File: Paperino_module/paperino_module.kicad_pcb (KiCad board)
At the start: 2 copper layers, 25.4 x 22 mm, 21 parts, among them P1 CONN_01X06, P2 CONN_01X06, P3 CONN_01X06, P4 CONN_01X06, Q1 PMOS, Q2 NMOS, U1 BMA250E, X1 XF2M-2615-1A, X2 XF2B-4545-1A

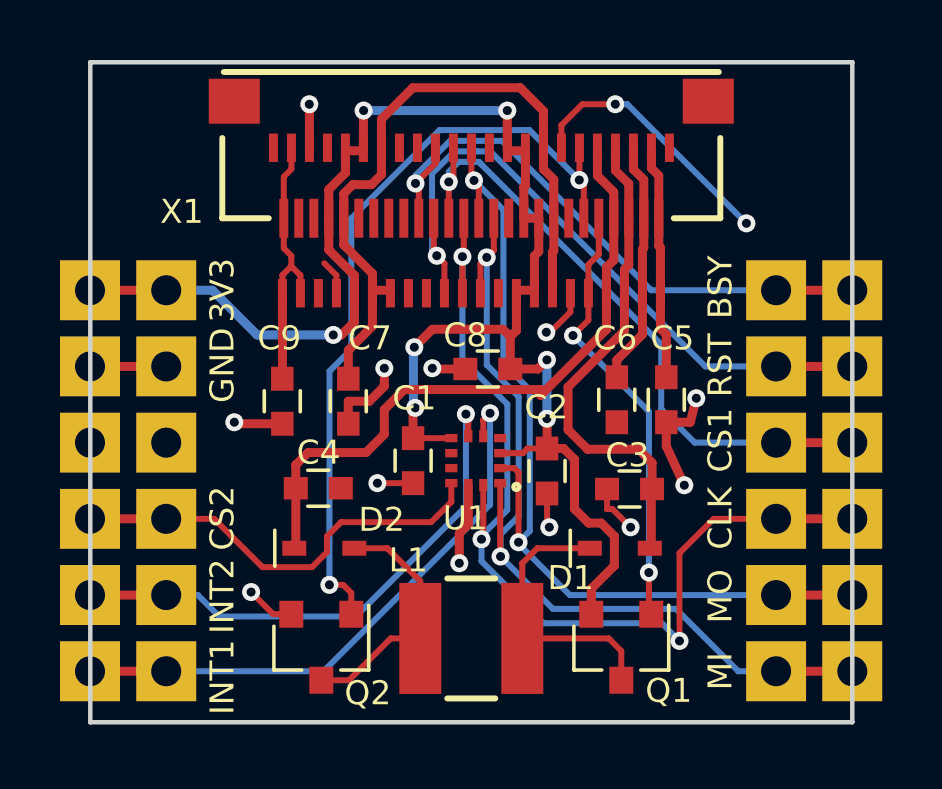
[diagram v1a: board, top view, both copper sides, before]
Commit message: more robust design for castellation
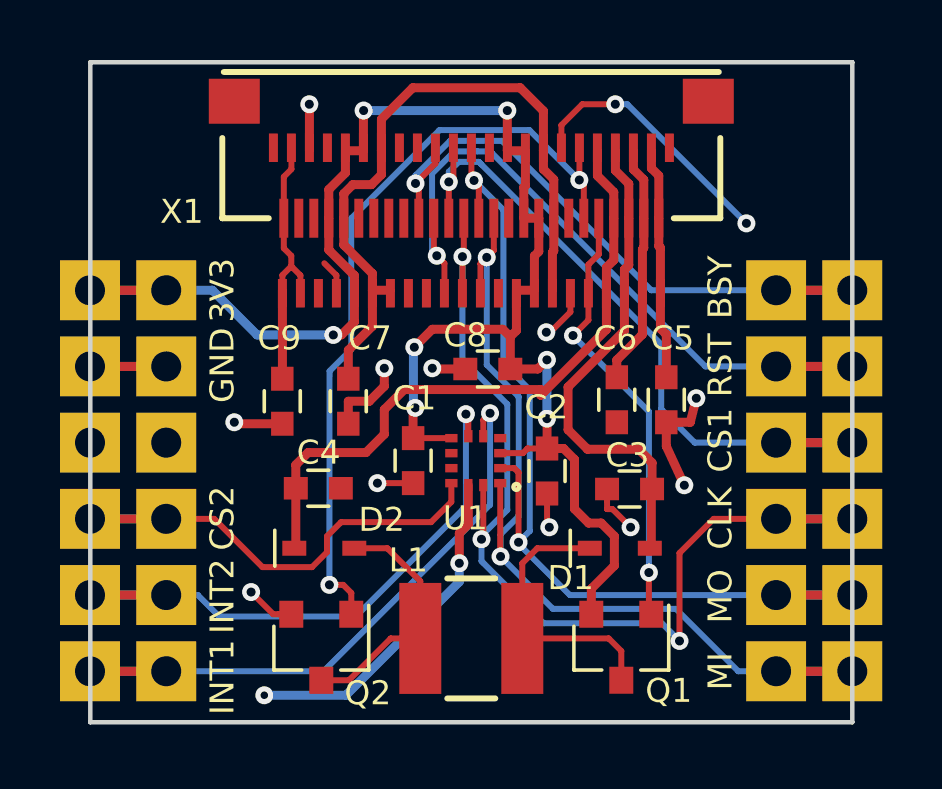
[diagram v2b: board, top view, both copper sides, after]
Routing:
- net GND: track 34.5 -> 45.7 mm, vias 14 -> 15
- net /INT2: track 18.2 -> 20.7 mm
- net /INT1: track 19.5 -> 22.1 mm
- net /SPI_CS2: track 14.5 -> 17.1 mm
- net /~RST: track 22.6 -> 25.2 mm
- net /~BUSY: track 19.9 -> 22.5 mm
- net /SPI_MOSI: track 30.2 -> 32.8 mm
- net /SPI_MISO: track 29.0 -> 31.5 mm
- net /SPI_CLK: track 32.2 -> 34.8 mm
- net +3V3: track 54.3 -> 56.9 mm
- net /SPI_CS1: track 21.4 -> 23.9 mm
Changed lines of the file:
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@@
     (thickness 1.6)
     (drawings 15)
-    (tracks 367)
+    (tracks 382)
     (zones 0)
     (modules 21)
@@
   )
   (setup
-    (last_trace_width 0.2)
+    (last_trace_width 0.3)
     (user_trace_width 0.2)
     (user_trace_width 0.3)
@@
   (gr_line (start 122.7 84.1) (end 148.1 84.1) (angle 90) (layer Edge.Cuts) (width 0.15))
   (gr_line (start 122.7 106.1) (end 122.7 84.1) (angle 90) (layer Edge.Cuts) (width 0.15))
+  (segment (start 125.23 91.7) (end 122.69 91.7) (width 0.3) (layer B.Cu) (net 1))
+  (segment (start 125.23 91.7) (end 122.69 91.7) (width 0.3) (layer F.Cu) (net 1))
   (segment (start 133.5 93.6) (end 133.47 93.63) (width 0.3) (layer B.Cu) (net 1))
   (via (at 133.5 93.6) (size 0.6) (drill 0.3) (layers F.Cu B.Cu) (net 1))
@@
   (segment (start 137.12 97.13) (end 137.275 96.975) (width 0.2) (layer F.Cu) (net 1))
   (segment (start 134.735 96.63) (end 133.46 96.63) (width 0.2) (layer F.Cu) (net 1) (status 30))
-  (segment (start 122.69 91.7) (end 125.23 91.7) (width 0.3) (layer F.Cu) (net 1) (status 30))
   (segment (start 137.504 91.7) (end 137.504 90.556) (width 0.3) (layer F.Cu) (net 1) (status 10))
   (segment (start 137.65 90.41) (end 137.65 89.3) (width 0.3) (layer F.Cu) (net 1) (status 20))
@@
   (segment (start 130.65 90.356398) (end 130.65 89.3) (width 0.3) (layer F.Cu) (net 1) (status 20))
   (segment (start 131.504 91.210398) (end 130.65 90.356398) (width 0.3) (layer F.Cu) (net 1))
+  (segment (start 125.23 94.24) (end 122.69 94.24) (width 0.3) (layer B.Cu) (net 2))
+  (segment (start 125.23 94.24) (end 122.69 94.24) (width 0.3) (layer F.Cu) (net 2))
+  (segment (start 135 100.8) (end 135 101.42) (width 0.3) (layer B.Cu) (net 2))
+  (segment (start 135.3 99.5) (end 135 99.8) (width 0.3) (layer F.Cu) (net 2))
+  (segment (start 135 99.8) (end 135 100.8) (width 0.3) (layer F.Cu) (net 2))
+  (via (at 135 100.8) (size 0.6) (drill 0.3) (layers F.Cu B.Cu) (net 2))
+  (segment (start 135.3 98.195) (end 135.3 99.5) (width 0.3) (layer F.Cu) (net 2) (status 10))
+  (via (at 128.5 105.2) (size 0.6) (drill 0.25) (layers F.Cu B.Cu) (net 2))
+  (segment (start 131.22 105.2) (end 128.5 105.2) (width 0.3) (layer B.Cu) (net 2))
+  (segment (start 135 101.42) (end 131.22 105.2) (width 0.3) (layer B.Cu) (net 2))
   (segment (start 138.704 91.7) (end 138.704 92.426) (width 0.2) (layer F.Cu) (net 2))
   (via (at 137.9 93.1) (size 0.6) (drill 0.3) (layers F.Cu B.Cu) (net 2))
@@
   (via (at 142.9 95.3) (size 0.6) (drill 0.3) (layers F.Cu B.Cu) (net 2))
   (segment (start 142.7 96.1) (end 142.9 95.3) (width 0.3) (layer F.Cu) (net 2))
-  (segment (start 135.3 98.195) (end 135.3 99.5) (width 0.3) (layer F.Cu) (net 2) (status 10))
-  (via (at 135 100.8) (size 0.6) (drill 0.3) (layers F.Cu B.Cu) (net 2))
-  (segment (start 135 99.8) (end 135 100.8) (width 0.3) (layer F.Cu) (net 2))
-  (segment (start 135.3 99.5) (end 135 99.8) (width 0.3) (layer F.Cu) (net 2))
   (segment (start 135.2 94.325) (end 134.125 94.325) (width 0.3) (layer F.Cu) (net 2) (status 10))
   (via (at 134.1 94.3) (size 0.6) (drill 0.3) (layers F.Cu B.Cu) (net 2))
@@
   (segment (start 137.925 99.525) (end 138 99.6) (width 0.2) (layer F.Cu) (net 2))
   (segment (start 139.925 98.325) (end 139.925 98.725) (width 0.2) (layer F.Cu) (net 2) (status 10))
-  (segment (start 122.69 94.24) (end 125.23 94.24) (width 0.3) (layer F.Cu) (net 2) (status 30))
   (segment (start 140.504 91.7) (end 140.504 93.046) (width 0.3) (layer F.Cu) (net 3) (status 10))
   (segment (start 141.425 97.45) (end 141.425 98.325) (width 0.3) (layer F.Cu) (net 3) (status 20))
@@
   (segment (start 133.7 103.306) (end 133.7 101.4) (width 0.2) (layer F.Cu) (net 10) (status 10))
   (segment (start 132.6 100.3) (end 131.5 100.3) (width 0.2) (layer F.Cu) (net 10) (status 20))
+  (segment (start 145.56 101.86) (end 148.1 101.86) (width 0.3) (layer B.Cu) (net 11) (status 30))
   (segment (start 136.975 100.1) (end 137.35 99.725) (width 0.2) (layer B.Cu) (net 11))
   (via (at 135.49 88.04) (size 0.6) (drill 0.3) (layers F.Cu B.Cu) (net 11))
@@
   (segment (start 135.404 87.954) (end 135.404 87.05) (width 0.2) (layer F.Cu) (net 11) (status 20))
   (segment (start 135.49 88.04) (end 135.404 87.954) (width 0.2) (layer F.Cu) (net 11))
+  (segment (start 145.56 104.4) (end 148.1 104.4) (width 0.3) (layer B.Cu) (net 12) (status 30))
   (segment (start 135.915 90.605) (end 135.915 94.185) (width 0.2) (layer B.Cu) (net 12))
   (segment (start 136.375 99.835) (end 136.375 100.575) (width 0.2) (layer B.Cu) (net 12))
@@
   (segment (start 135.704 90.816) (end 135.915 90.605) (width 0.2) (layer F.Cu) (net 12))
   (segment (start 135.915 90.605) (end 136.15 90.37) (width 0.2) (layer F.Cu) (net 12))
+  (segment (start 145.56 99.32) (end 148.1 99.32) (width 0.3) (layer B.Cu) (net 13) (status 30))
   (segment (start 135.74 99.885) (end 136.6 99.025) (width 0.2) (layer B.Cu) (net 13))
   (via (at 135.104 90.58) (size 0.6) (drill 0.3) (layers F.Cu B.Cu) (net 13))
@@
   (segment (start 135.104 91.7) (end 135.104 90.58) (width 0.2) (layer F.Cu) (net 13) (status 10))
   (segment (start 145.56 99.32) (end 148.1 99.32) (width 0.3) (layer F.Cu) (net 13) (status 30))
+  (segment (start 145.56 96.78) (end 148.1 96.78) (width 0.3) (layer B.Cu) (net 14) (status 30))
   (segment (start 134.65 88.09) (end 134.65 87.749956) (width 0.2) (layer B.Cu) (net 14))
   (segment (start 135.73 87.5) (end 141.73 93.5) (width 0.2) (layer B.Cu) (net 14))
@@
   (segment (start 134.65 88.09) (end 134.65 89.3) (width 0.2) (layer F.Cu) (net 14) (status 20))
   (segment (start 134.804 87.936) (end 134.65 88.09) (width 0.2) (layer F.Cu) (net 14))
+  (segment (start 145.56 94.24) (end 148.1 94.24) (width 0.3) (layer B.Cu) (net 15) (status 30))
   (segment (start 136.08 87.12) (end 136.079998 87.12) (width 0.2) (layer B.Cu) (net 15))
   (segment (start 145.56 94.24) (end 143.2 94.24) (width 0.2) (layer B.Cu) (net 15) (status 20))
@@
   (segment (start 134.504 90.804) (end 134.27 90.57) (width 0.2) (layer F.Cu) (net 15))
   (segment (start 134.27 90.57) (end 134.15 90.45) (width 0.2) (layer F.Cu) (net 15))
+  (segment (start 145.56 91.7) (end 148.1 91.7) (width 0.3) (layer B.Cu) (net 16) (status 30))
   (segment (start 133.65 89.3) (end 133.65 88.25) (width 0.2) (layer F.Cu) (net 16) (status 10))
   (segment (start 133.65 88.25) (end 133.54 88.14) (width 0.2) (layer F.Cu) (net 16))
@@
   (segment (start 134.204 87.476) (end 133.54 88.14) (width 0.2) (layer F.Cu) (net 16))
   (segment (start 145.56 91.7) (end 148.1 91.7) (width 0.3) (layer F.Cu) (net 16) (status 30))
+  (segment (start 122.69 99.32) (end 125.23 99.32) (width 0.3) (layer B.Cu) (net 18) (status 30))
   (segment (start 125.23 99.32) (end 126.83 99.32) (width 0.2) (layer F.Cu) (net 18))
   (segment (start 134.735 98.755) (end 134.735 98.13) (width 0.2) (layer F.Cu) (net 18))
@@
   (segment (start 126.83 99.32) (end 128.44 100.93) (width 0.2) (layer F.Cu) (net 18))
   (segment (start 122.69 99.32) (end 125.23 99.32) (width 0.3) (layer F.Cu) (net 18) (status 30))
+  (segment (start 122.69 101.86) (end 125.23 101.86) (width 0.3) (layer B.Cu) (net 19) (status 30))
   (segment (start 135.3 96.565) (end 135.3 95.91) (width 0.2) (layer F.Cu) (net 19))
   (segment (start 135.22 98.905) (end 135.1025 99.0225) (width 0.2) (layer B.Cu) (net 19))
@@
   (segment (start 131.55 102.575) (end 127 102.575) (width 0.2) (layer B.Cu) (net 19))
   (segment (start 122.69 101.86) (end 125.23 101.86) (width 0.3) (layer F.Cu) (net 19) (status 30))
+  (segment (start 122.69 104.4) (end 125.23 104.4) (width 0.3) (layer B.Cu) (net 20) (status 30))
   (segment (start 125.23 104.4) (end 130.475 104.4) (width 0.2) (layer B.Cu) (net 20) (status 10))
   (segment (start 135.8 96.025) (end 136.025 95.8) (width 0.2) (layer F.Cu) (net 20))
